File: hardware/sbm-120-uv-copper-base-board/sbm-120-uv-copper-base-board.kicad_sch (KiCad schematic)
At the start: 5 parts, among them J1 +, J2 THERMISTOR, J3 -, U1 SBM-120-UV

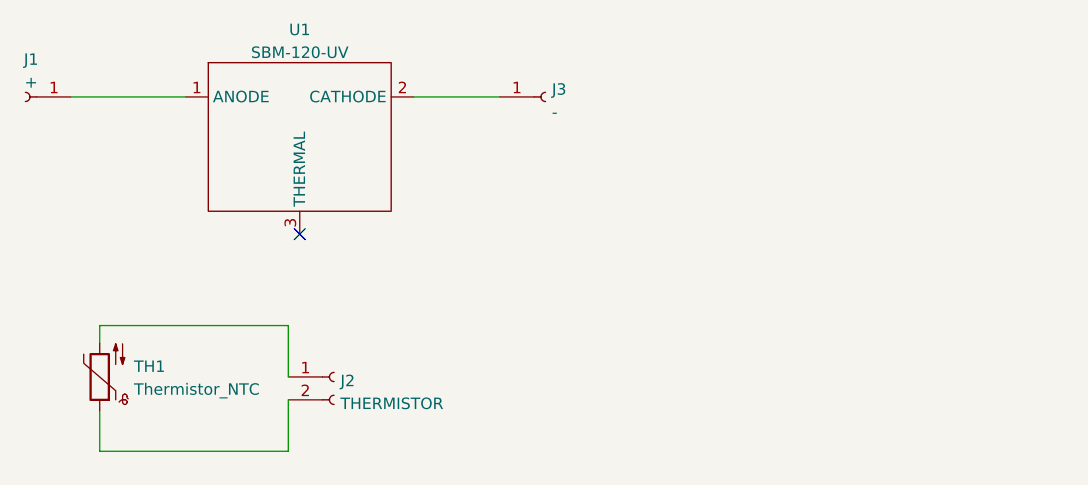
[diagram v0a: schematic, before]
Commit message: single led copper base + uven pocket finished
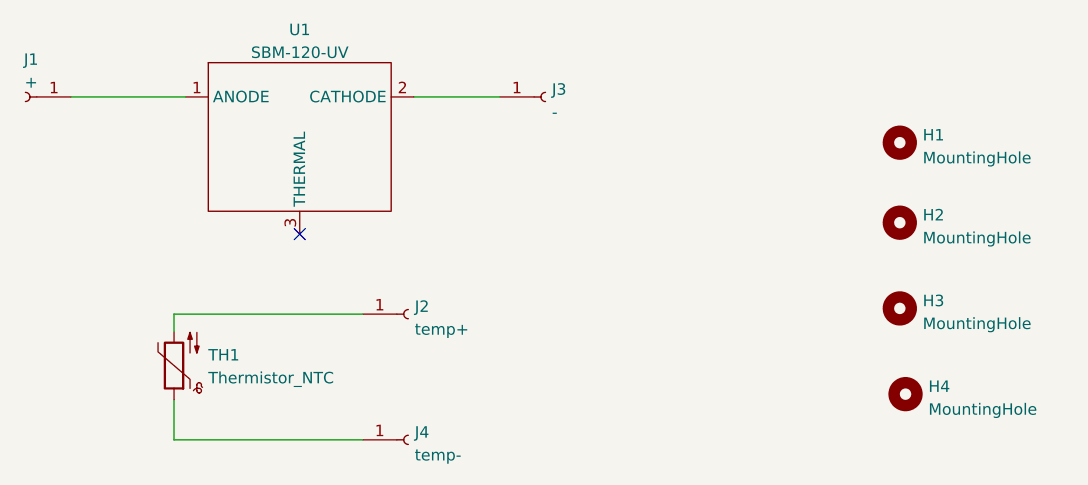
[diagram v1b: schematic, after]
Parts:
- removed J2: THERMISTOR, TestPoint:TestPoint_2Pads_Pitch2.54mm_Drill0.8mm, symbol Connector:Conn_01x02_Female
- added H1, H2, H3, H4: MountingHole, MountingHole:MountingHole_3.2mm_M3, symbol Mechanical:MountingHole
- added J2: temp+, TestPoint:TestPoint_Pad_1.5x1.5mm, symbol Connector:Conn_01x01_Female
- added J4: temp-, TestPoint:TestPoint_Pad_1.5x1.5mm, symbol Connector:Conn_01x01_Female
- TH1: footprint Resistor_SMD:R_0603_1608Metric -> Resistor_SMD:R_0805_2012Metric_Pad1.20x1.40mm_HandSolder
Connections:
- net at TH1.2: now also J2.1 (Pin_1)
- net at TH1.1: now also J4.1 (Pin_1)
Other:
- moved on the sheet: TH1
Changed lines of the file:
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@@
     (stroke (width 0) (type default) (color 0 0 0 0))
   )
-  (wire (pts (xy 102.235 96.52) (xy 102.235 94.615))
-    (stroke (width 0) (type default) (color 0 0 0 0))
-  )
-  (wire (pts (xy 123.19 102.87) (xy 123.19 108.585))
+  (wire (pts (xy 110.49 95.25) (xy 110.49 93.345))
     (stroke (width 0) (type default) (color 0 0 0 0))
   )
@@
     (stroke (width 0) (type default) (color 0 0 0 0))
   )
-  (wire (pts (xy 102.235 108.585) (xy 102.235 104.14))
-    (stroke (width 0) (type default) (color 0 0 0 0))
-  )
-  (wire (pts (xy 123.19 94.615) (xy 123.19 100.33))
-    (stroke (width 0) (type default) (color 0 0 0 0))
-  )
-  (wire (pts (xy 102.235 94.615) (xy 123.19 94.615))
-    (stroke (width 0) (type default) (color 0 0 0 0))
-  )
-  (wire (pts (xy 123.19 108.585) (xy 102.235 108.585))
+  (wire (pts (xy 110.49 107.315) (xy 110.49 102.87))
+    (stroke (width 0) (type default) (color 0 0 0 0))
+  )
+  (wire (pts (xy 110.49 93.345) (xy 131.445 93.345))
+    (stroke (width 0) (type default) (color 0 0 0 0))
+  )
+  (wire (pts (xy 131.445 107.315) (xy 110.49 107.315))
     (stroke (width 0) (type default) (color 0 0 0 0))
   )
@@
     (pin "1")
   )
-  (symbol (lib_id "Connector:Conn_01x02_Female") (at 128.27 100.33 0) (unit 1)
-    (in_bom yes) (on_board yes) (fields_autoplaced)
-    (property "Reference" "J2" (id 0) (at 128.9812 100.7653 0)
-      (effects (font (size 1.27 1.27)) (justify left))
-    )
-    (property "Value" "THERMISTOR" (id 1) (at 128.9812 103.3022 0)
-      (effects (font (size 1.27 1.27)) (justify left))
-    )
-    (property "Footprint" "TestPoint:TestPoint_2Pads_Pitch2.54mm_Drill0.8mm" (id 2) (at 128.27 100.33 0)
-      (effects (font (size 1.27 1.27)) hide)
-    )
-    (property "Datasheet" "~" (id 3) (at 128.27 100.33 0)
-      (effects (font (size 1.27 1.27)) hide)
-    )
-    (pin "1")
-    (pin "2")
-  )
-  (symbol (lib_id "Device:Thermistor_NTC") (at 102.235 100.33 180) (unit 1)
-    (in_bom yes) (on_board yes) (fields_autoplaced)
-    (property "Reference" "TH1" (id 0) (at 106.045 99.1778 0)
+  (symbol (lib_id "Connector:Conn_01x01_Female") (at 136.525 93.345 0) (unit 1)
+    (in_bom yes) (on_board yes) (fields_autoplaced)
+    (property "Reference" "J2" (id 0) (at 137.2362 92.5103 0)
+      (effects (font (size 1.27 1.27)) (justify left))
+    )
+    (property "Value" "temp+" (id 1) (at 137.2362 95.0472 0)
+      (effects (font (size 1.27 1.27)) (justify left))
+    )
+    (property "Footprint" "TestPoint:TestPoint_Pad_1.5x1.5mm" (id 2) (at 136.525 93.345 0)
+      (effects (font (size 1.27 1.27)) hide)
+    )
+    (property "Datasheet" "~" (id 3) (at 136.525 93.345 0)
+      (effects (font (size 1.27 1.27)) hide)
+    )
+    (pin "1")
+  )
+  (symbol (lib_id "Mechanical:MountingHole") (at 191.135 92.71 0) (unit 1)
+    (in_bom yes) (on_board yes) (fields_autoplaced)
+    (property "Reference" "H3" (id 0) (at 193.675 91.8753 0)
+      (effects (font (size 1.27 1.27)) (justify left))
+    )
+    (property "Value" "MountingHole" (id 1) (at 193.675 94.4122 0)
+      (effects (font (size 1.27 1.27)) (justify left))
+    )
+    (property "Footprint" "MountingHole:MountingHole_3.2mm_M3" (id 2) (at 191.135 92.71 0)
+      (effects (font (size 1.27 1.27)) hide)
+    )
+    (property "Datasheet" "~" (id 3) (at 191.135 92.71 0)
+      (effects (font (size 1.27 1.27)) hide)
+    )
+  )
+  (symbol (lib_id "Device:Thermistor_NTC") (at 110.49 99.06 180) (unit 1)
+    (in_bom yes) (on_board yes) (fields_autoplaced)
+    (property "Reference" "TH1" (id 0) (at 114.3 97.9078 0)
       (effects (font (size 1.27 1.27)) (justify right))
     )
-    (property "Value" "Thermistor_NTC" (id 1) (at 106.045 101.7147 0)
+    (property "Value" "Thermistor_NTC" (id 1) (at 114.3 100.4447 0)
       (effects (font (size 1.27 1.27)) (justify right))
     )
-    (property "Footprint" "Resistor_SMD:R_0603_1608Metric" (id 2) (at 102.235 101.6 0)
-      (effects (font (size 1.27 1.27)) hide)
-    )
-    (property "Datasheet" "~" (id 3) (at 102.235 101.6 0)
+    (property "Footprint" "Resistor_SMD:R_0805_2012Metric_Pad1.20x1.40mm_HandSolder" (id 2) (at 110.49 100.33 0)
+      (effects (font (size 1.27 1.27)) hide)
+    )
+    (property "Datasheet" "~" (id 3) (at 110.49 100.33 0)
       (effects (font (size 1.27 1.27)) hide)
     )
@@
     (pin "3")
   )
+  (symbol (lib_id "Mechanical:MountingHole") (at 191.135 74.295 0) (unit 1)
+    (in_bom yes) (on_board yes) (fields_autoplaced)
+    (property "Reference" "H1" (id 0) (at 193.675 73.4603 0)
+      (effects (font (size 1.27 1.27)) (justify left))
+    )
+    (property "Value" "MountingHole" (id 1) (at 193.675 75.9972 0)
+      (effects (font (size 1.27 1.27)) (justify left))
+    )
+    (property "Footprint" "MountingHole:MountingHole_3.2mm_M3" (id 2) (at 191.135 74.295 0)
+      (effects (font (size 1.27 1.27)) hide)
+    )
+    (property "Datasheet" "~" (id 3) (at 191.135 74.295 0)
+      (effects (font (size 1.27 1.27)) hide)
+    )
+  )
+  (symbol (lib_id "Connector:Conn_01x01_Female") (at 136.525 107.315 0) (unit 1)
+    (in_bom yes) (on_board yes) (fields_autoplaced)
+    (property "Reference" "J4" (id 0) (at 137.2362 106.4803 0)
+      (effects (font (size 1.27 1.27)) (justify left))
+    )
+    (property "Value" "temp-" (id 1) (at 137.2362 109.0172 0)
+      (effects (font (size 1.27 1.27)) (justify left))
+    )
+    (property "Footprint" "TestPoint:TestPoint_Pad_1.5x1.5mm" (id 2) (at 136.525 107.315 0)
+      (effects (font (size 1.27 1.27)) hide)
+    )
+    (property "Datasheet" "~" (id 3) (at 136.525 107.315 0)
+      (effects (font (size 1.27 1.27)) hide)
+    )
+    (pin "1")
+  )
+  (symbol (lib_id "Mechanical:MountingHole") (at 191.135 83.185 0) (unit 1)
+    (in_bom yes) (on_board yes) (fields_autoplaced)
+    (property "Reference" "H2" (id 0) (at 193.675 82.3503 0)
+      (effects (font (size 1.27 1.27)) (justify left))
+    )
+    (property "Value" "MountingHole" (id 1) (at 193.675 84.8872 0)
+      (effects (font (size 1.27 1.27)) (justify left))
+    )
+    (property "Footprint" "MountingHole:MountingHole_3.2mm_M3" (id 2) (at 191.135 83.185 0)
+      (effects (font (size 1.27 1.27)) hide)
+    )
+    (property "Datasheet" "~" (id 3) (at 191.135 83.185 0)
+      (effects (font (size 1.27 1.27)) hide)
+    )
+  )
+  (symbol (lib_id "Mechanical:MountingHole") (at 191.77 102.235 0) (unit 1)
+    (in_bom yes) (on_board yes) (fields_autoplaced)
+    (property "Reference" "H4" (id 0) (at 194.31 101.4003 0)
+      (effects (font (size 1.27 1.27)) (justify left))
+    )
+    (property "Value" "MountingHole" (id 1) (at 194.31 103.9372 0)
+      (effects (font (size 1.27 1.27)) (justify left))
+    )
+    (property "Footprint" "MountingHole:MountingHole_3.2mm_M3" (id 2) (at 191.77 102.235 0)
+      (effects (font (size 1.27 1.27)) hide)
+    )
+    (property "Datasheet" "~" (id 3) (at 191.77 102.235 0)
+      (effects (font (size 1.27 1.27)) hide)
+    )
+  )
   (symbol (lib_id "Connector:Conn_01x01_Female") (at 93.98 69.215 180) (unit 1)
     (in_bom yes) (on_board yes) (fields_autoplaced)
@@
   )
   (symbol_instances
+    (path "/86053866-715e-4d2b-95ca-99641aa9854d"
+      (reference "H1") (unit 1) (value "MountingHole") (footprint "MountingHole:MountingHole_3.2mm_M3")
+    )
+    (path "/c6967526-0ad6-4fd6-9437-faa5c2a98dfa"
+      (reference "H2") (unit 1) (value "MountingHole") (footprint "MountingHole:MountingHole_3.2mm_M3")
+    )
+    (path "/3129dec1-45cd-4636-b0db-870d96ea7225"
+      (reference "H3") (unit 1) (value "MountingHole") (footprint "MountingHole:MountingHole_3.2mm_M3")
+    )
+    (path "/d16153bf-afe3-44f5-8253-8a23df02086e"
+      (reference "H4") (unit 1) (value "MountingHole") (footprint "MountingHole:MountingHole_3.2mm_M3")
+    )
     (path "/f9ae4293-c3d4-430d-a2aa-a3274f0ce623"
       (reference "J1") (unit 1) (value "+") (footprint "TestPoint:TestPoint_Pad_3.0x3.0mm")
     )
-    (path "/4e51af3c-4afe-4f92-af56-6bf0683cd7a5"
-      (reference "J2") (unit 1) (value "THERMISTOR") (footprint "TestPoint:TestPoint_2Pads_Pitch2.54mm_Drill0.8mm")
+    (path "/1ecbc2c0-0eaa-47b8-8f34-84976ac3dad6"
+      (reference "J2") (unit 1) (value "temp+") (footprint "TestPoint:TestPoint_Pad_1.5x1.5mm")
     )
     (path "/08d64b05-4362-4511-864e-8594a18d6ecd"
       (reference "J3") (unit 1) (value "-") (footprint "TestPoint:TestPoint_Pad_3.0x3.0mm")
     )
+    (path "/961be747-2ec7-43a8-ad5e-fa403e84ec03"
+      (reference "J4") (unit 1) (value "temp-") (footprint "TestPoint:TestPoint_Pad_1.5x1.5mm")
+    )
     (path "/73e9e27e-ac85-4818-bdc2-1ca9effb8f8b"
-      (reference "TH1") (unit 1) (value "Thermistor_NTC") (footprint "Resistor_SMD:R_0603_1608Metric")
+      (reference "TH1") (unit 1) (value "Thermistor_NTC") (footprint "Resistor_SMD:R_0805_2012Metric_Pad1.20x1.40mm_HandSolder")
     )
     (path "/8044f456-889d-4378-8989-06f76d6098bd"
